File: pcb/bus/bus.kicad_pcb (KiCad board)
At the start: 2 copper layers, 170 x 55 mm, 0 parts

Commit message: update pcb limits and add other pcb setup
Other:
- copper layers 2 -> 4
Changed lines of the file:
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@@
 	(generator_version "8.0")
 	(general
-		(thickness 1.6)
+		(thickness 1.6062)
 		(legacy_teardrops no)
 	)
@@
 	(layers
 		(0 "F.Cu" signal)
+		(1 "In1.Cu" power)
+		(2 "In2.Cu" power)
 		(31 "B.Cu" signal)
 		(32 "B.Adhes" user "B.Adhesive")
@@
 	)
 	(setup
+		(stackup
+			(layer "F.SilkS"
+				(type "Top Silk Screen")
+				(color "White")
+			)
+			(layer "F.Paste"
+				(type "Top Solder Paste")
+			)
+			(layer "F.Mask"
+				(type "Top Solder Mask")
+				(color "Green")
+				(thickness 0.01)
+			)
+			(layer "F.Cu"
+				(type "copper")
+				(thickness 0.035)
+			)
+			(layer "dielectric 1"
+				(type "prepreg")
+				(color "FR4 natural")
+				(thickness 0.2104)
+				(material "FR4")
+				(epsilon_r 4.4)
+				(loss_tangent 0.02)
+			)
+			(layer "In1.Cu"
+				(type "copper")
+				(thickness 0.0152)
+			)
+			(layer "dielectric 2"
+				(type "core")
+				(color "FR4 natural")
+				(thickness 1.065)
+				(material "FR4")
+				(epsilon_r 4.6)
+				(loss_tangent 0.02)
+			)
+			(layer "In2.Cu"
+				(type "copper")
+				(thickness 0.0152)
+			)
+			(layer "dielectric 3"
+				(type "prepreg")
+				(color "FR4 natural")
+				(thickness 0.2104)
+				(material "FR4")
+				(epsilon_r 4.4)
+				(loss_tangent 0.02)
+			)
+			(layer "B.Cu"
+				(type "copper")
+				(thickness 0.035)
+			)
+			(layer "B.Mask"
+				(type "Bottom Solder Mask")
+				(color "Green")
+				(thickness 0.01)
+			)
+			(layer "B.Paste"
+				(type "Bottom Solder Paste")
+			)
+			(layer "B.SilkS"
+				(type "Bottom Silk Screen")
+				(color "White")
+			)
+			(copper_finish "ENIG")
+			(dielectric_constraints yes)
+		)
 		(pad_to_mask_clearance 0)
 		(allow_soldermask_bridges_in_footprints no)

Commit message: update bus pcb
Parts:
- added C101: 10uF, Capacitor_SMD:C_0805_2012Metric, F.Cu at (114.2, 33.4)
- added C102: 10uF, Capacitor_SMD:C_0805_2012Metric, F.Cu at (115.8, 44.1)
- added C103: 100nF, Capacitor_SMD:C_0805_2012Metric, F.Cu at (115.8, 47.1)
- added H101: MountingHole_Pad, MountingHole:MountingHole_3.2mm_M3_Pad_Via, F.Cu at (59.8, 65.8)
- added H102: MountingHole_Pad, MountingHole:MountingHole_3.2mm_M3_Pad_Via, F.Cu at (59.8, 135.8)
- added H103: MountingHole_Pad, MountingHole:MountingHole_3.2mm_M3_Pad_Via, F.Cu at (219.8, 135.8)
- added H104: MountingHole_Pad, MountingHole:MountingHole_3.2mm_M3_Pad_Via, F.Cu at (219.8, 65.8)
- added H201: MountingHole_Pad, MountingHole:MountingHole_3.2mm_M3_Pad_Via, F.Cu at (75.6, 67.0)
- added H202: MountingHole_Pad, MountingHole:MountingHole_3.2mm_M3_Pad_Via, F.Cu at (76.0, 135.3)
- added H301: MountingHole_Pad, MountingHole:MountingHole_3.2mm_M3_Pad_Via, F.Cu at (96.5, 67.8)
- added H302: MountingHole_Pad, MountingHole:MountingHole_3.2mm_M3_Pad_Via, F.Cu at (95.3, 135.5)
- added H401: MountingHole_Pad, MountingHole:MountingHole_3.2mm_M3_Pad_Via, F.Cu at (116.8, 67.8)
- added H402: MountingHole_Pad, MountingHole:MountingHole_3.2mm_M3_Pad_Via, F.Cu at (116.3, 134.7)
- added H501: MountingHole_Pad, MountingHole:MountingHole_3.2mm_M3_Pad_Via, F.Cu at (135.6, 68.9)
- added H502: MountingHole_Pad, MountingHole:MountingHole_3.2mm_M3_Pad_Via, F.Cu at (137.3, 134.6)
- added H601: MountingHole_Pad, MountingHole:MountingHole_3.2mm_M3_Pad_Via, F.Cu at (157.0, 69.2)
- added H602: MountingHole_Pad, MountingHole:MountingHole_3.2mm_M3_Pad_Via, F.Cu at (156.8, 134.4)
- added H701: MountingHole_Pad, MountingHole:MountingHole_3.2mm_M3_Pad_Via, F.Cu at (177.5, 67.4)
- added H702: MountingHole_Pad, MountingHole:MountingHole_3.2mm_M3_Pad_Via, F.Cu at (178.4, 134.6)
- added J201: Conn_02x10_Row_Letter_First, PRJ:PCN10-20P-2.54DSA, F.Cu at (75.1, 89.4)
- added J301: Conn_02x10_Row_Letter_First, PRJ:PCN10-20P-2.54DSA, F.Cu at (95.4, 89.4)
- added J401: Conn_02x10_Row_Letter_First, PRJ:PCN10-20P-2.54DSA, F.Cu at (115.8, 89.4)
- added J501: Conn_02x10_Row_Letter_First, PRJ:PCN10-20P-2.54DSA, F.Cu at (136.1, 89.4)
- added J601: Conn_02x10_Row_Letter_First, PRJ:PCN10-20P-2.54DSA, F.Cu at (156.4, 89.4)
- added J701: Conn_02x10_Row_Letter_First, PRJ:PCN10-20P-2.54DSA, F.Cu at (176.7, 89.4)
- added R101: 2k7, Resistor_SMD:R_0805_2012Metric, F.Cu at (107.8, 52.5)
- added R102: R/C/0Ohm, Resistor_SMD:R_0805_2012Metric, F.Cu at (65.2, 65.9)
- added R103: R/C/0Ohm, Resistor_SMD:R_0805_2012Metric, F.Cu at (65.2, 135.8)
- added R104: R/C/0Ohm, Resistor_SMD:R_0805_2012Metric, F.Cu at (214.3, 135.8)
- added R105: R/C/0Ohm, Resistor_SMD:R_0805_2012Metric, F.Cu at (214.3, 65.9)
- added U101: USBLC6-2SC6, Package_TO_SOT_SMD:SOT-666, F.Cu at (115.6, 50.4)
- added U102: FE1.1s, Package_SO:SSOP-28_3.9x9.9mm_P0.635mm, F.Cu at (109.6, 45.3)
- added Y101: 12MHz, PRJ:M49S-SMD, F.Cu at (113.2, 56.2)
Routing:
- added copper zone on In1.Cu, net GND
- added copper zone on In2.Cu, net GND
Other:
- board size 170 x 55 mm -> 170 x 80 mm

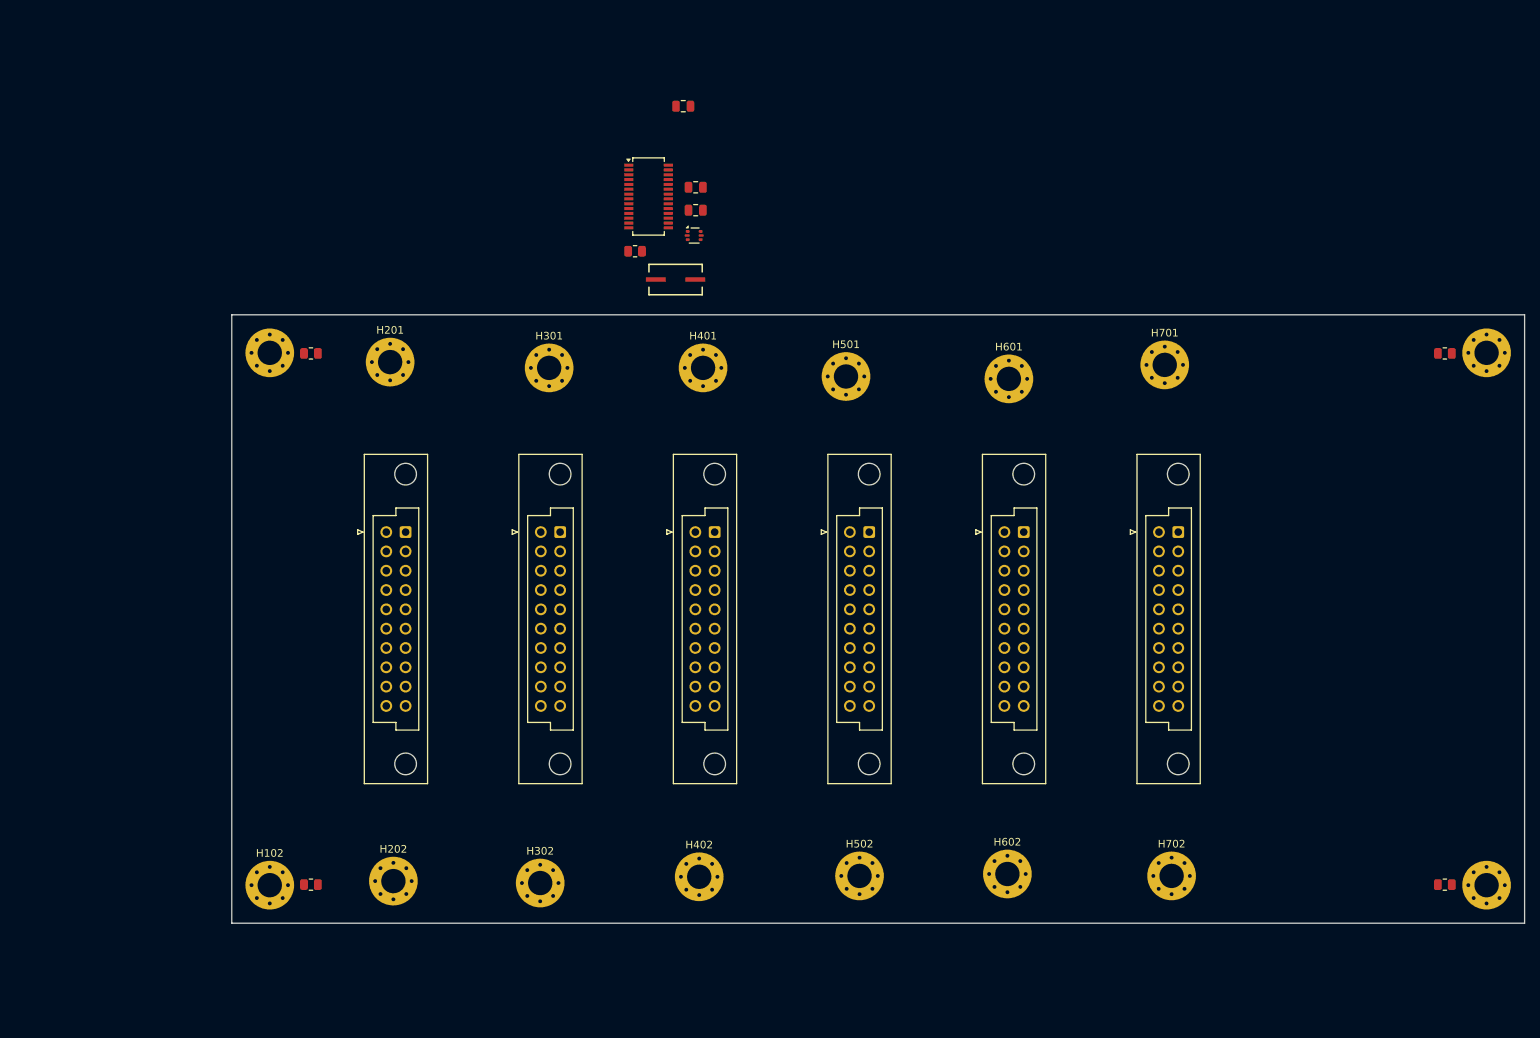
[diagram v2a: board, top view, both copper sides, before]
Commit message: update pcb size
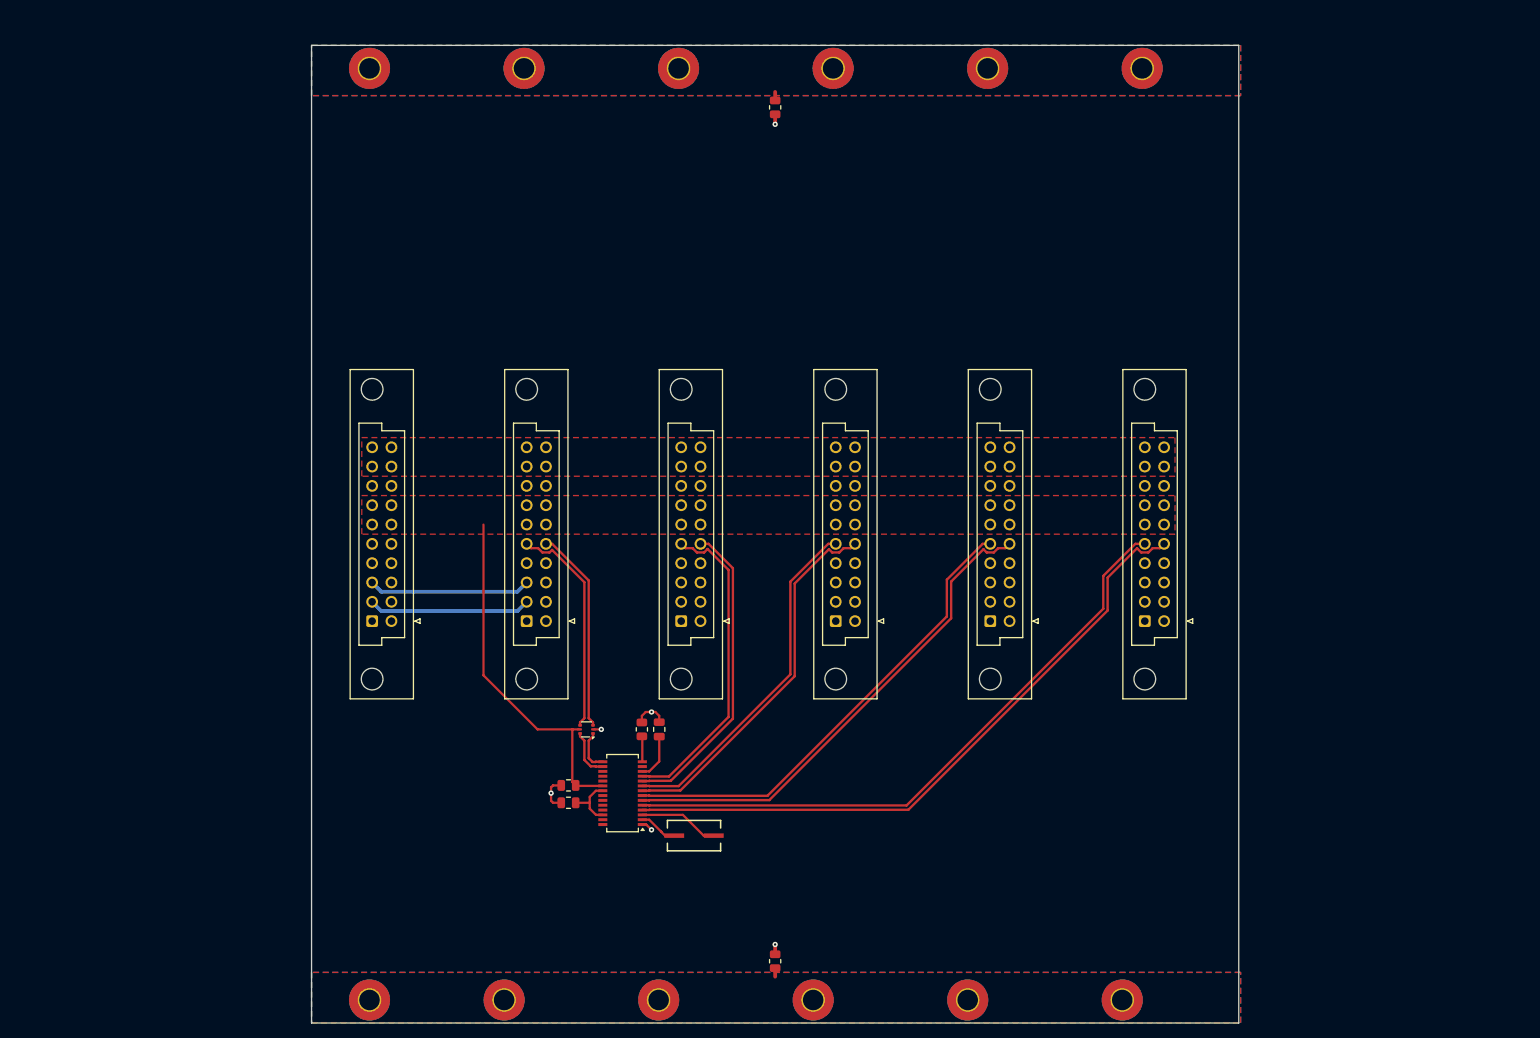
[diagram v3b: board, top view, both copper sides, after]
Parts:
- removed the H103 at (219.8, 135.8)
- removed the H104 at (219.8, 65.8)
- removed H701, H702: MountingHole_Pad, MountingHole:MountingHole_3.2mm_M3_Pad_Via
- removed R104, R105: R/C/0Ohm, Resistor_SMD:R_0805_2012Metric
- H101: footprint MountingHole:MountingHole_3.2mm_M3_Pad_Via -> MountingHole:MountingHole_2.7mm_M2.5_Pad_TopBottom
- H102: renamed from H201; footprint MountingHole:MountingHole_3.2mm_M3_Pad_Via -> MountingHole:MountingHole_2.7mm_M2.5_Pad_TopBottom
- H103: renamed from H301; footprint MountingHole:MountingHole_3.2mm_M3_Pad_Via -> MountingHole:MountingHole_2.7mm_M2.5_Pad_TopBottom
- H104: renamed from H401; footprint MountingHole:MountingHole_3.2mm_M3_Pad_Via -> MountingHole:MountingHole_2.7mm_M2.5_Pad_TopBottom
- H105: renamed from H501; footprint MountingHole:MountingHole_3.2mm_M3_Pad_Via -> MountingHole:MountingHole_2.7mm_M2.5_Pad_TopBottom
- H106: renamed from H601; footprint MountingHole:MountingHole_3.2mm_M3_Pad_Via -> MountingHole:MountingHole_2.7mm_M2.5_Pad_TopBottom
- H109: renamed from H102; footprint MountingHole:MountingHole_3.2mm_M3_Pad_Via -> MountingHole:MountingHole_2.7mm_M2.5_Pad_TopBottom
- H110: renamed from H202; footprint MountingHole:MountingHole_3.2mm_M3_Pad_Via -> MountingHole:MountingHole_2.7mm_M2.5_Pad_TopBottom
- H111: renamed from H302; footprint MountingHole:MountingHole_3.2mm_M3_Pad_Via -> MountingHole:MountingHole_2.7mm_M2.5_Pad_TopBottom
- H112: renamed from H402; footprint MountingHole:MountingHole_3.2mm_M3_Pad_Via -> MountingHole:MountingHole_2.7mm_M2.5_Pad_TopBottom
- H113: renamed from H502; footprint MountingHole:MountingHole_3.2mm_M3_Pad_Via -> MountingHole:MountingHole_2.7mm_M2.5_Pad_TopBottom
- H114: renamed from H602; footprint MountingHole:MountingHole_3.2mm_M3_Pad_Via -> MountingHole:MountingHole_2.7mm_M2.5_Pad_TopBottom
- R101: value 2k7 -> R/C/0Ohm
- R103: value R/C/0Ohm -> 2k7
- moved R102 100.6 mm to (126.2, 145.8), turned to -90 degrees
- moved C101 92.8 mm to (99.1, 125.0), turned to 180 degrees
- moved U102 78.5 mm to (106.2, 123.7), turned to 180 degrees
- moved C103 77.5 mm to (99.1, 122.7), turned to 180 degrees
- moved Y101 73.2 mm to (115.6, 129.3), turned to 180 degrees
- moved C102 71.4 mm to (111.0, 115.3), turned to 90 degrees
- moved U101 66.5 mm to (101.4, 115.3), turned to 180 degrees
- moved R103 48.1 mm to (108.7, 115.3), turned to 90 degrees
- moved H105 44.6 mm to (154.2, 28.4)
- moved H106 44.4 mm to (174.5, 28.4)
- moved H104 42.9 mm to (133.9, 28.4)
- moved H103 42.9 mm to (113.5, 28.4)
- moved H102 42.4 mm to (93.2, 28.4)
- moved H101 39.6 mm to (72.9, 28.4)
- moved R101 26.4 mm to (126.2, 33.5), turned to 90 degrees
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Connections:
- H101 pad 1: Net-(H101-Pad1) -> /GND_TOP_MH
- H102 pad 1: GND -> /GND_TOP_MH
- H103 pad 1: GND -> /GND_TOP_MH
- H104 pad 1: GND -> /GND_TOP_MH
- H105 pad 1: GND -> /GND_TOP_MH
- H106 pad 1: GND -> /GND_TOP_MH
- H109 pad 1: Net-(H102-Pad1) -> /GND_BOTTOM_MH
- H110 pad 1: GND -> /GND_BOTTOM_MH
- H111 pad 1: GND -> /GND_BOTTOM_MH
- H112 pad 1: GND -> /GND_BOTTOM_MH
- H113 pad 1: GND -> /GND_BOTTOM_MH
- H114 pad 1: GND -> /GND_BOTTOM_MH
- R101 pad 1: Net-(U102-REXT) -> GND
- R101 pad 2: GND -> /GND_TOP_MH
- R102 pad 2: Net-(H101-Pad1) -> /GND_BOTTOM_MH
- R103 pad 1: GND -> Net-(U102-REXT)
- R103 pad 2: Net-(H102-Pad1) -> GND
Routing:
- net /USB4-: track 0.00 -> 86.1 mm
- net /USB4+: track 0.00 -> 82.9 mm
- net /USB3-: track 0.00 -> 65.4 mm
- net /USB3+: track 0.00 -> 62.3 mm
- net /USB2-: track 0.00 -> 48.9 mm
- net +5V: track 0.00 -> 46.5 mm
- net /USB2+: track 0.00 -> 45.8 mm
- net /USB1+: track 0.00 -> 41.9 mm
- net /USB1-: track 0.00 -> 40.7 mm
- net /MASTER_USB+: track 0.00 -> 29.0 mm
- net /MASTER_USB-: track 0.00 -> 26.9 mm
- net /I2C_SDA: track 0.00 -> 21.3 mm
- net /I2C_SCL: track 0.00 -> 21.3 mm
- net GND: track 0.00 -> 14.2 mm, vias 0 -> 6
- net Net-(U102-XIN): track 0.00 -> 10.5 mm
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- added copper zone on F.Cu, net +12V
- added copper zone on F.Cu, net +5V
- added copper zone on B.Cu, net /GND_BOTTOM_MH
- added copper zone on F.Cu, net /GND_BOTTOM_MH
- added copper zone on B.Cu, net /GND_TOP_MH
- added copper zone on F.Cu, net /GND_TOP_MH
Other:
- board size 170 x 80 mm -> 121.9 x 128.6 mm

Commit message: fix unconnected
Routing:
- net /VD33: track 7.49 -> 15.0 mm
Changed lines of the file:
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@@
+	)
+	(segment
+		(start 103.578 123.4025)
+		(end 104.4635 123.4025)
+		(width 0.3)
+		(layer "F.Cu")
+		(net 2)
 	)
 	(segment
 		(start 100.016 124.99)
 		(end 101.86 124.99)
+		(width 0.3)
+		(layer "F.Cu")
+		(net 2)
+	)
+	(segment
+		(start 104.4635 123.4025)
+		(end 104.908 122.958)
 		(width 0.3)
 		(layer "F.Cu")
@@
 	)
 	(segment
+		(start 103.578 121.4975)
+		(end 104.8445 121.4975)
+		(width 0.3)
+		(layer "F.Cu")
+		(net 2)
+	)
+	(segment
 		(start 101.86 124.99)
 		(end 101.86 125.752)
@@
 	)
 	(segment
+		(start 104.908 122.958)
+		(end 104.908 122.196)
+		(width 0.3)
+		(layer "F.Cu")
+		(net 2)
+	)
+	(segment
+		(start 104.908 122.196)
+		(end 104.908 121.434)
+		(width 0.3)
+		(layer "F.Cu")
+		(net 2)
+	)
+	(segment
 		(start 101.86 124.2205)
 		(end 101.86 124.99)
+		(width 0.3)
+		(layer "F.Cu")
+		(net 2)
+	)
+	(segment
+		(start 104.8445 121.4975)
+		(end 104.908 121.434)
 		(width 0.3)
 		(layer "F.Cu")
@@
 	)
 	(segment
+		(start 104.908 121.18)
+		(end 104.5905 120.8625)
+		(width 0.3)
+		(layer "F.Cu")
+		(net 2)
+	)
+	(segment
+		(start 104.5905 120.8625)
+		(end 103.578 120.8625)
+		(width 0.3)
+		(layer "F.Cu")
+		(net 2)
+	)
+	(segment
 		(start 102.678 123.4025)
 		(end 101.86 124.2205)
 		(width 0.3)
 		(layer "F.Cu")
+		(net 2)
+	)
+	(segment
+		(start 103.578 122.1325)
+		(end 104.8445 122.1325)
+		(width 0.3)
+		(layer "F.Cu")
+		(net 2)
+	)
+	(segment
+		(start 104.908 121.434)
+		(end 104.908 121.18)
+		(width 0.3)
+		(layer "F.Cu")
+		(net 2)
+	)
+	(segment
+		(start 104.8445 122.1325)
+		(end 104.908 122.196)
+		(width 0.3)
+		(layer "F.Cu")

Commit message: update bus pcb
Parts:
- added C104: 100nF, Capacitor_SMD:C_0805_2012Metric, F.Cu at (101.1, 83.3)
- added C105: 100nF, Capacitor_SMD:C_0805_2012Metric, F.Cu at (121.2, 83.3)
- added C106: 100nF, Capacitor_SMD:C_0805_2012Metric, F.Cu at (127.0, 83.3)
- added C107: 100nF, Capacitor_SMD:C_0805_2012Metric, F.Cu at (146.8, 83.3)
- added C108: 100nF, Capacitor_SMD:C_0805_2012Metric, F.Cu at (166.9, 83.3)
- added U103: USBLC6-2SC6, Package_TO_SOT_SMD:SOT-666, F.Cu at (120.1, 80.3)
- added U104: USBLC6-2SC6, Package_TO_SOT_SMD:SOT-666, F.Cu at (127.8, 80.3)
- added U105: USBLC6-2SC6, Package_TO_SOT_SMD:SOT-666, F.Cu at (147.8, 80.3)
- added U106: USBLC6-2SC6, Package_TO_SOT_SMD:SOT-666, F.Cu at (167.9, 80.3)
- moved U101 35.1 mm to (100.1, 80.3), turned to -90 degrees
- moved R102 32.5 mm to (123.7, 113.5)
- moved H110 30.9 mm to (95.3, 120.4)
- moved H111 30.8 mm to (115.3, 120.4)
- moved H112 30.8 mm to (135.3, 120.4)
- moved H113 30.8 mm to (155.3, 120.4)
- moved H114 30.7 mm to (175.3, 120.4)
- moved H109 30.6 mm to (75.3, 120.4)
- moved Y101 17.4 mm to (117.9, 112.0)
- moved C101 15.0 mm to (98.6, 110.0)
- moved C103 15.0 mm to (98.6, 107.7)
- moved U102 15.0 mm to (105.7, 108.7)
- moved J701 14.4 mm to (175.3, 86.8)
- moved J601 14.4 mm to (155.3, 86.8)
- moved J501 14.4 mm to (135.3, 86.8)
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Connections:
- J201 pad a5: /MASTER_USB+ -> /RPI Connector/NS_USB+
- J201 pad b5: /MASTER_USB- -> /RPI Connector/NS_USB-
- J401 pad a5: /USB1+ -> /Device Connector 1/NS_USB+
- J401 pad b5: /USB1- -> /Device Connector 1/NS_USB-
- J501 pad a5: /USB2+ -> /Device Connector 2/NS_USB+
- J501 pad b5: /USB2- -> /Device Connector 2/NS_USB-
- J601 pad a5: /USB3+ -> /Device Connector 3/NS_USB+
- J601 pad b5: /USB3- -> /Device Connector 3/NS_USB-
- J701 pad a5: /USB4+ -> /Device Connector 4/NS_USB+
- J701 pad b5: /USB4- -> /Device Connector 4/NS_USB-
- U101 pad 1: /MASTER_USB_F- -> /RPI Connector/NS_USB-
- U101 pad 3: /MASTER_USB- -> /RPI Connector/NS_USB+
- U101 pad 6: /MASTER_USB_F+ -> /MASTER_USB-
- U102 pad 15: /MASTER_USB_F- -> /MASTER_USB-
- U102 pad 16: /MASTER_USB_F+ -> /MASTER_USB+
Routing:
- net +5V: track 46.5 -> 89.7 mm, vias 0 -> 10
- net /USB2-: track 48.9 -> 37.4 mm
- net /USB1+: track 41.9 -> 31.3 mm
- net /USB2+: track 45.8 -> 36.1 mm
- net GND: track 14.2 -> 23.4 mm, vias 6 -> 15
- net /Device Connector 2/NS_USB-: track 0.00 -> 8.85 mm
- net /RPI Connector/NS_USB+: track 0.00 -> 8.56 mm
- net /Device Connector 4/NS_USB-: track 0.00 -> 8.54 mm
- net /USB3-: track 65.4 -> 56.9 mm
- net /Device Connector 3/NS_USB-: track 0.00 -> 8.46 mm
- net /USB1-: track 40.7 -> 32.2 mm
- net /USB4-: track 86.1 -> 77.8 mm
- net /Device Connector 1/NS_USB+: track 0.00 -> 8.13 mm
- net /Device Connector 2/NS_USB+: track 0.00 -> 7.55 mm
- net /Device Connector 3/NS_USB+: track 0.00 -> 7.48 mm
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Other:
- board size 121.9 x 128.6 mm -> 117.4 x 100 mm

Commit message: fix
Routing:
- net +5V: track 89.7 -> 90.6 mm
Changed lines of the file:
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@@
+	)
+	(via
+		(at 127.006 74.164)
+		(size 0.7)
+		(drill 0.3)
+		(layers "F.Cu" "B.Cu")
+		(net 4)
 	)
 	(via
@@
 	)
 	(via
-		(at 100.59 74.672)
-		(size 0.7)
-		(drill 0.3)
-		(layers "F.Cu" "B.Cu")
-		(net 4)
-	)
-	(via
-		(at 147.326 74.164)
+		(at 100.844 74.164)
 		(size 0.7)
 		(drill 0.3)
@@
 	(via
 		(at 147.834 82.038)
+		(size 0.7)
+		(drill 0.3)
+		(layers "F.Cu" "B.Cu")
+		(net 4)
+	)
+	(via
+		(at 167.138 74.164)
 		(size 0.7)
 		(drill 0.3)
@@
 	)
 	(via
-		(at 167.392 74.164)
-		(size 0.7)
-		(drill 0.3)
-		(layers "F.Cu" "B.Cu")
-		(net 4)
-	)
-	(via
-		(at 127.26 74.164)
+		(at 147.072 74.164)
 		(size 0.7)
 		(drill 0.3)
@@
 	)
 	(segment
+		(start 167.138 81.022)
+		(end 167.138 74.164)
+		(width 0.5)
+		(layer "B.Cu")
+		(net 4)
+	)
+	(segment
 		(start 167.9 81.784)
 		(end 167.392 81.276)
@@
 	)
 	(segment
-		(start 100.59 81.269047)
-		(end 100.59 74.672)
+		(start 127.006 81.022)
+		(end 127.006 74.164)
 		(width 0.5)
 		(layer "B.Cu")
@@
 	)
 	(segment
-		(start 147.326 81.276)
-		(end 147.326 74.164)
+		(start 100.844 81.015047)
+		(end 100.844 74.164)
 		(width 0.5)
 		(layer "B.Cu")
@@
 	)
 	(segment
+		(start 147.072 81.022)
+		(end 147.072 74.164)
+		(width 0.5)
+		(layer "B.Cu")
+		(net 4)
+	)
+	(segment
 		(start 120.91 80.9925)
 		(end 120.91 74.164)
+		(width 0.5)
+		(layer "B.Cu")
+		(net 4)
+	)
+	(segment
+		(start 127.26 81.276)
+		(end 127.006 81.022)
+		(width 0.5)
+		(layer "B.Cu")
+		(net 4)
+	)
+	(segment
+		(start 167.392 81.276)
+		(end 167.138 81.022)
 		(width 0.5)
 		(layer "B.Cu")
@@
 	)
 	(segment
-		(start 127.768 82.038)
-		(end 127.768 81.784)
+		(start 147.326 81.276)
+		(end 147.072 81.022)
 		(width 0.5)
 		(layer "B.Cu")
@@
 	)
 	(segment
-		(start 127.26 81.276)
-		(end 127.26 74.164)
+		(start 100.59 81.269047)
+		(end 100.844 81.015047)
+		(width 0.5)
+		(layer "B.Cu")
+		(net 4)
+	)
+	(segment
+		(start 127.768 82.038)
+		(end 127.768 81.784)
 		(width 0.5)
 		(layer "B.Cu")
@@
 		(width 0.5)
 		(layer "B.Cu")
-		(net 4)
-	)
-	(segment
-		(start 167.392 81.276)
-		(end 167.392 74.164)
-		(width 0.5)
-		(layer "B.Cu")
